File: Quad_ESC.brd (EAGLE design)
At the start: 96.5 x 39.9 mm, 28 parts, among them Y1 ECS-80-S-4X

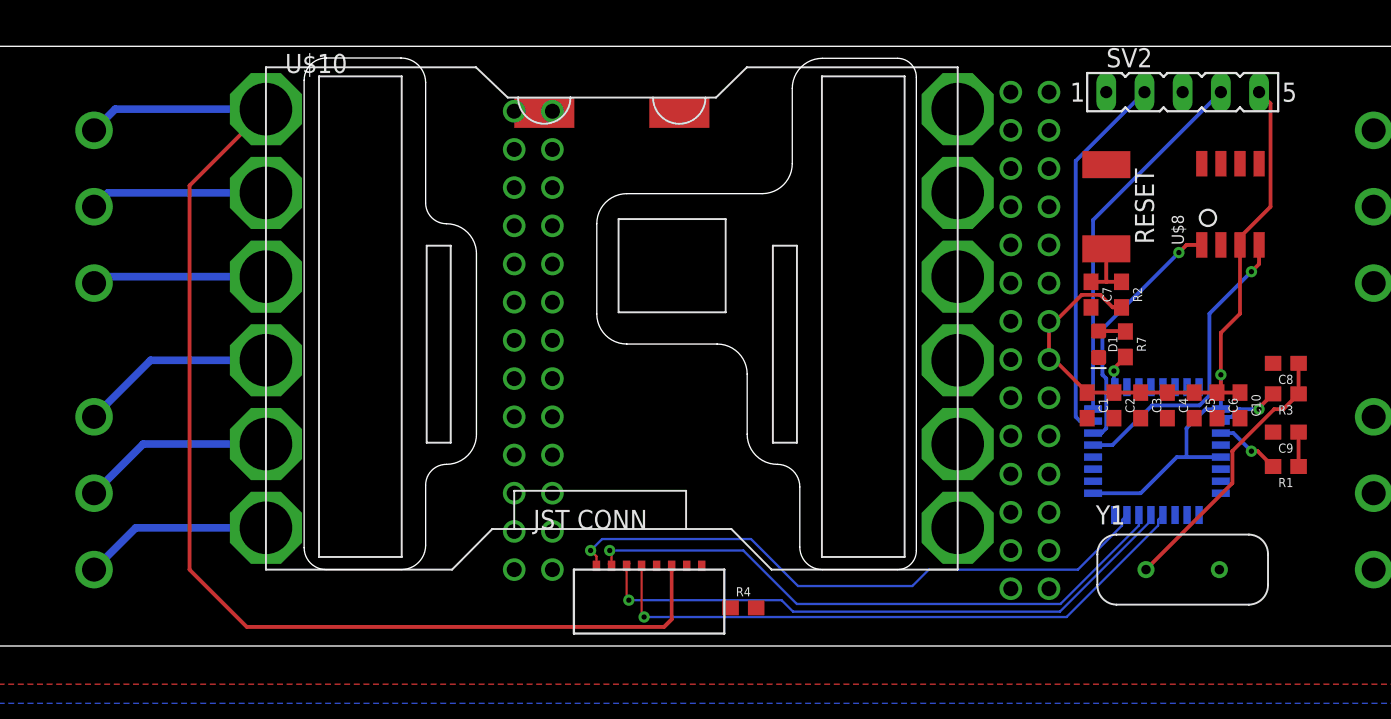
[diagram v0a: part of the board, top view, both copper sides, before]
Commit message: Quick Board Update
ripup; done for presentation, only placement of components present on board
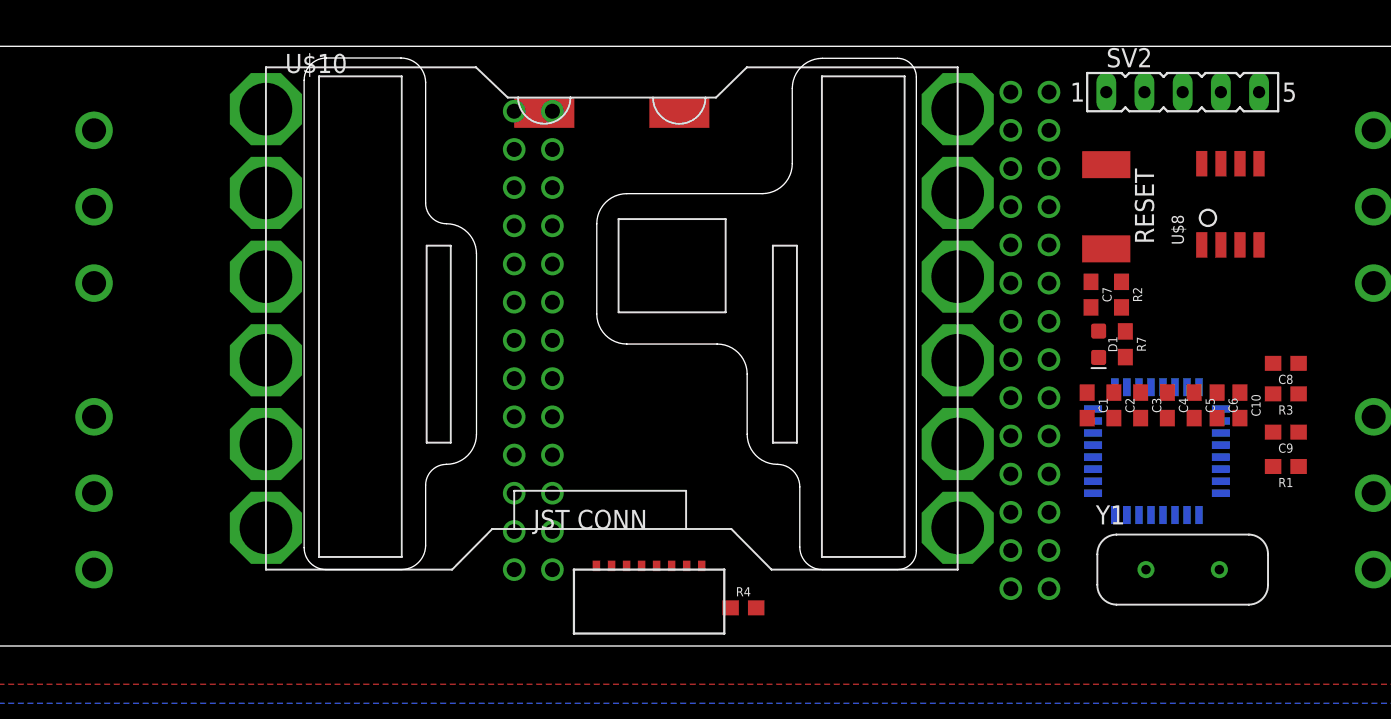
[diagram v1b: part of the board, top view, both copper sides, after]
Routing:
- net ESC1_B: track 82.1 -> 0.00 mm
- net +3V3: track 60.3 -> 0.00 mm, vias 1 -> 0
- net TIM3_CH1: track 41.0 -> 0.00 mm, vias 1 -> 0
- net TIM3_CH3: track 40.8 -> 0.00 mm, vias 1 -> 0
- net TIM3_CH4: track 40.6 -> 0.00 mm, vias 1 -> 0
- net TIM3_CH2: track 40.5 -> 0.00 mm, vias 1 -> 0
- net SWDIO: track 24.8 -> 0.00 mm
- net SWCLK: track 24.6 -> 0.00 mm
- net CAN_RX: track 20.5 -> 0.00 mm, vias 1 -> 0
- net N$2: track 18.3 -> 0.00 mm
- net CAN_TX: track 16.6 -> 0.00 mm, vias 1 -> 0
- net ESC2_B: track 13.0 -> 0.00 mm
- net ESC2_Y: track 12.8 -> 0.00 mm
- net ESC2_R: track 12.6 -> 0.00 mm
- net ESC1_Y: track 11.8 -> 0.00 mm
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
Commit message: Update Quad_ESC.brd
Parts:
- moved U$2 64.2 mm to (14.0, 3.05), turned to 180 degrees
- moved R4 36.2 mm to (85.3, 7.87)
- moved U$7 24.6 mm to (66.8, 10.2)
- moved U$6 24.4 mm to (67.1, 29.2)
- moved Y1 14.6 mm to (92.2, 10.7), turned to 270 degrees
- moved U$9 7.89 mm to (40.6, 7.11)
- moved U$10 4.44 mm to (13.5, 6.10)
- moved U$4 0.51 mm to (81.8, 10.2)
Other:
- board size 96.5 x 39.9 mm -> 96.5 x 40.1 mm

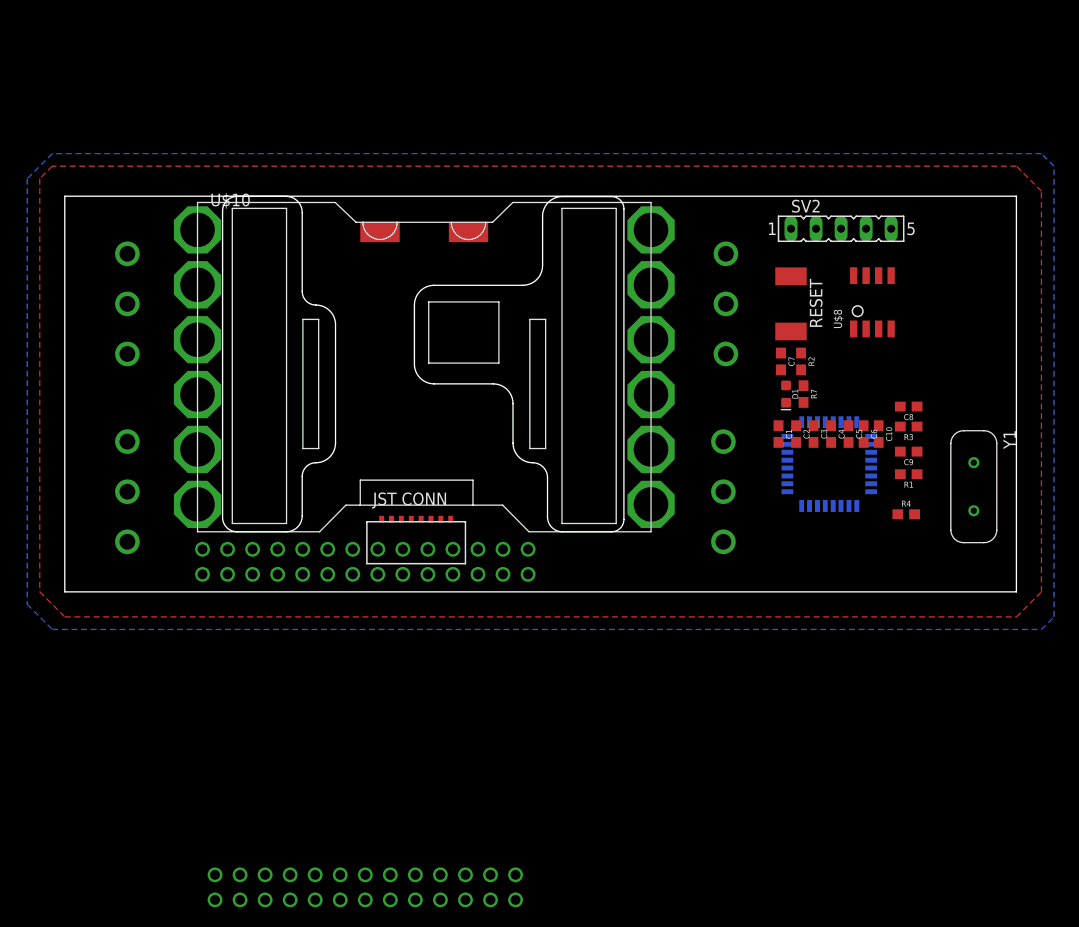
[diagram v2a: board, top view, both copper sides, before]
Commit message: Board/Schem Update
added CLT low profile samtec connectors to schem/board, looking at the connector spacing on the board stresses me out ;-;
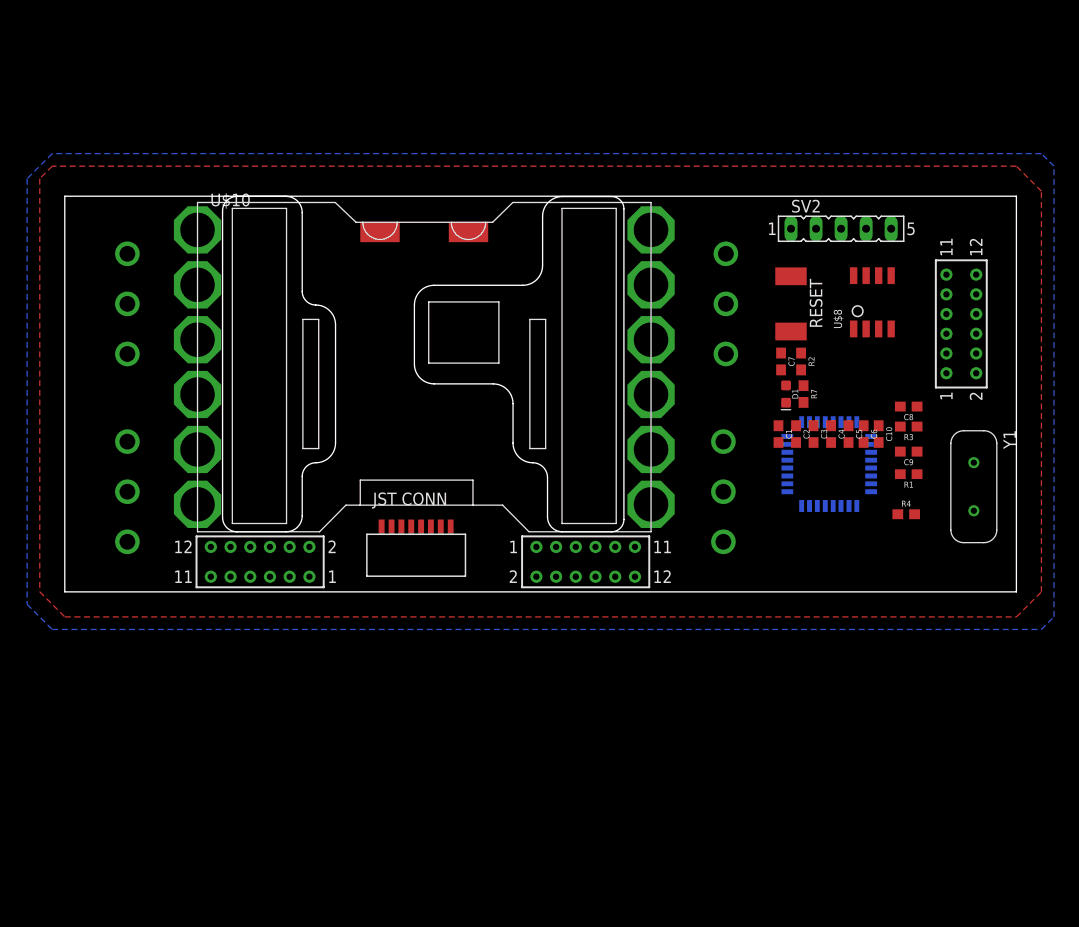
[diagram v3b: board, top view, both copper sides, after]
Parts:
- removed U$9: 8PIN_CONNECTOR, BLHeli_32 45A:8PI_CONNECTOR
- added J1, J2, J3: SAMTEC-CLT-106-01-X-DJ, BLHeli_32 45A:SAMTEC-CLT-106-01-X-D
- U$2: value ESC2BACKPLANE -> 8PIN_CONNECTOR; device ESC_to_Backplane_Connectors:ESC2BACKPLANE_WHOLE -> BLHeli_32 45A:8PI_CONNECTOR
- moved U$2 26.8 mm to (40.6, 5.84), flipped to the top
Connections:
- removed net N$10: U$2.P$7
- removed net N$6: U$9.P$4
- removed net N$9: U$2.P$6
- removed net PROG_SEL: U$2.P$5
- net +12V: now also J1.1, J1.2, J1.3, J1.4, J1.5, J1.6, J1.7, J1.8, J2.1, J2.2, J2.3, J2.4, J2.5, J2.6, J2.7, J2.8; no longer U$2.P$10, U$2.P$11, U$2.P$12, U$2.P$13, U$2.P$23, U$2.P$24, U$2.P$25, U$2.P$26, U$2.P$27, U$2.P$9, U$2.P$A, U$2.P$B, U$2.P$C, U$2.P$D, U$2.P$E, U$2.P$O, U$2.P$P, U$2.P$Q, U$2.P$R, U$2.P$S
- net +3V3: now also J3.1, J3.2, J3.3, J3.4; no longer U$2.P$G, U$2.P$H, U$2.P$U, U$2.P$V
- net CAN_H: now also J3.7
- net CAN_L: now also J3.9
- net ESC1_B: no longer U$9.P$3
- net GND: now also J1.10, J1.11, J1.12, J1.9, J2.10, J2.11, J2.12, J2.9; no longer U$2.P$1, U$2.P$15, U$2.P$16, U$2.P$17, U$2.P$18, U$2.P$2, U$2.P$3, U$2.P$4, U$2.P$AA, U$2.P$BB, U$2.P$J, U$2.P$K, U$2.P$L, U$2.P$M, U$2.P$N, U$2.P$X, U$2.P$Y, U$2.P$Z, U$9.P$1, U$9.P$2
- net TIM3_CH1: no longer U$9.P$5
- net TIM3_CH2: no longer U$9.P$6
- net TIM3_CH3: no longer U$9.P$7
- net TIM3_CH4: no longer U$9.P$8

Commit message: Board Update
actually put the connectors on the right side of the board this time haha
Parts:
- moved J2 0.76 mm to (19.1, 3.05), flipped to the bottom, turned to 0 degrees
- moved J3 0.57 mm to (91.4, 27.4), flipped to the bottom
- moved J1 0.25 mm to (53.1, 3.05), flipped to the bottom, turned to 180 degrees
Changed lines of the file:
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@@
 <attribute name="VALUE" x="85.344" y="7.112" size="0.6096" layer="27" font="vector" ratio="20" align="top-center"/>
 </element>
-<element name="J2" library="BLHeli_32 45A" package="SAMTEC-CLT-106-01-X-D" value="SAMTEC-CLT-106-01-X-DJ" x="19.812" y="3.048" smashed="yes" rot="R180">
-<attribute name="VALUE" x="19.812" y="3.748" size="0.635" layer="27" rot="R180" align="bottom-center"/>
-</element>
-<element name="J3" library="BLHeli_32 45A" package="SAMTEC-CLT-106-01-X-D" value="SAMTEC-CLT-106-01-X-DJ" x="90.932" y="27.178" smashed="yes" rot="R90">
-<attribute name="VALUE" x="91.632" y="27.178" size="0.635" layer="27" rot="R90" align="bottom-center"/>
+<element name="J2" library="BLHeli_32 45A" package="SAMTEC-CLT-106-01-X-D" value="SAMTEC-CLT-106-01-X-DJ" x="19.05" y="3.048" smashed="yes" rot="MR0">
+<attribute name="VALUE" x="19.05" y="2.348" size="0.635" layer="28" rot="MR0" align="bottom-center"/>
+</element>
+<element name="J3" library="BLHeli_32 45A" package="SAMTEC-CLT-106-01-X-D" value="SAMTEC-CLT-106-01-X-DJ" x="91.44" y="27.432" smashed="yes" rot="MR90">
+<attribute name="VALUE" x="90.74" y="27.432" size="0.635" layer="28" rot="MR90" align="bottom-center"/>
 </element>
 <element name="U$2" library="BLHeli_32 45A" package="8PI_CONNECTOR" value="8PIN_CONNECTOR" x="40.64" y="5.842" smashed="yes" rot="R180"/>
-<element name="J1" library="BLHeli_32 45A" package="SAMTEC-CLT-106-01-X-D" value="SAMTEC-CLT-106-01-X-DJ" x="52.832" y="3.048" smashed="yes">
-<attribute name="VALUE" x="53.086" y="2.348" size="0.635" layer="27" align="bottom-center"/>
+<element name="J1" library="BLHeli_32 45A" package="SAMTEC-CLT-106-01-X-D" value="SAMTEC-CLT-106-01-X-DJ" x="53.086" y="3.048" smashed="yes" rot="MR180">
+<attribute name="VALUE" x="53.34" y="3.748" size="0.635" layer="28" rot="MR180" align="bottom-center"/>
 </element>
 </elements>
@@
 <wire x1="86.194" y1="7.874" x2="80.338" y2="8.71" width="0" layer="19" extent="1-16"/>
 <wire x1="31.972" y1="36.466" x2="73.66" y2="32.01" width="0" layer="19" extent="1-1"/>
-<wire x1="14.812" y1="1.537" x2="31.972" y2="36.466" width="0" layer="19" extent="1-1"/>
-<wire x1="16.812" y1="1.537" x2="14.812" y2="1.537" width="0" layer="19" extent="1-1"/>
-<wire x1="16.812" y1="4.559" x2="16.812" y2="1.537" width="0" layer="19" extent="1-1"/>
-<wire x1="14.812" y1="4.559" x2="16.812" y2="4.559" width="0" layer="19" extent="1-1"/>
-<wire x1="55.832" y1="4.559" x2="16.812" y2="4.559" width="0" layer="19" extent="1-1"/>
-<wire x1="57.832" y1="4.559" x2="55.832" y2="4.559" width="0" layer="19" extent="1-1"/>
-<wire x1="55.832" y1="1.537" x2="55.832" y2="4.559" width="0" layer="19" extent="1-1"/>
-<wire x1="57.832" y1="1.537" x2="55.832" y2="1.537" width="0" layer="19" extent="1-1"/>
+<wire x1="14.05" y1="4.559" x2="31.972" y2="36.466" width="0" layer="19" extent="1-1"/>
+<wire x1="16.05" y1="4.559" x2="14.05" y2="4.559" width="0" layer="19" extent="1-1"/>
+<wire x1="16.05" y1="1.537" x2="16.05" y2="4.559" width="0" layer="19" extent="1-1"/>
+<wire x1="14.05" y1="1.537" x2="16.05" y2="1.537" width="0" layer="19" extent="1-1"/>
+<wire x1="56.086" y1="1.537" x2="16.05" y2="1.537" width="0" layer="19" extent="1-1"/>
+<wire x1="58.086" y1="1.537" x2="56.086" y2="1.537" width="0" layer="19" extent="1-1"/>
+<wire x1="56.086" y1="4.559" x2="56.086" y2="1.537" width="0" layer="19" extent="1-1"/>
+<wire x1="58.086" y1="4.559" x2="56.086" y2="4.559" width="0" layer="19" extent="1-1"/>
 </signal>
 <signal name="+3V3">
@@
 <wire x1="81.788" y1="12.56" x2="81.788" y2="15.76" width="0" layer="19" extent="16-16"/>
 <wire x1="73.288" y1="10.16" x2="74.168" y2="16.852" width="0" layer="19" extent="1-16"/>
-<wire x1="89.421" y1="24.178" x2="73.288" y2="10.16" width="0" layer="19" extent="16-16"/>
-<wire x1="89.421" y1="22.178" x2="89.421" y2="24.178" width="0" layer="19" extent="1-1"/>
-<wire x1="92.443" y1="22.178" x2="89.421" y2="22.178" width="0" layer="19" extent="1-1"/>
-<wire x1="92.443" y1="24.178" x2="92.443" y2="22.178" width="0" layer="19" extent="1-1"/>
+<wire x1="92.951" y1="24.432" x2="73.288" y2="10.16" width="0" layer="19" extent="16-16"/>
+<wire x1="92.951" y1="22.432" x2="92.951" y2="24.432" width="0" layer="19" extent="1-1"/>
+<wire x1="89.929" y1="22.432" x2="92.951" y2="22.432" width="0" layer="19" extent="1-1"/>
+<wire x1="89.929" y1="24.432" x2="89.929" y2="22.432" width="0" layer="19" extent="1-1"/>
 </signal>
 <signal name="CAN_TX">
@@
 <contactref element="J1" pad="5"/>
 <contactref element="J1" pad="7"/>
-<wire x1="18.812" y1="1.537" x2="40.952" y2="36.466" width="0" layer="19" extent="1-1"/>
-<wire x1="20.812" y1="1.537" x2="18.812" y2="1.537" width="0" layer="19" extent="1-1"/>
-<wire x1="22.812" y1="1.537" x2="20.812" y2="1.537" width="0" layer="19" extent="1-1"/>
-<wire x1="24.812" y1="1.537" x2="22.812" y2="1.537" width="0" layer="19" extent="1-1"/>
-<wire x1="24.812" y1="4.559" x2="24.812" y2="1.537" width="0" layer="19" extent="1-1"/>
-<wire x1="22.812" y1="4.559" x2="24.812" y2="4.559" width="0" layer="19" extent="1-1"/>
-<wire x1="20.812" y1="4.559" x2="22.812" y2="4.559" width="0" layer="19" extent="1-1"/>
-<wire x1="18.812" y1="4.559" x2="20.812" y2="4.559" width="0" layer="19" extent="1-1"/>
-<wire x1="47.832" y1="4.559" x2="24.812" y2="4.559" width="0" layer="19" extent="1-1"/>
-<wire x1="49.832" y1="4.559" x2="47.832" y2="4.559" width="0" layer="19" extent="1-1"/>
-<wire x1="51.832" y1="4.559" x2="49.832" y2="4.559" width="0" layer="19" extent="1-1"/>
-<wire x1="53.832" y1="4.559" x2="51.832" y2="4.559" width="0" layer="19" extent="1-1"/>
-<wire x1="47.832" y1="1.537" x2="47.832" y2="4.559" width="0" layer="19" extent="1-1"/>
-<wire x1="49.832" y1="1.537" x2="47.832" y2="1.537" width="0" layer="19" extent="1-1"/>
-<wire x1="51.832" y1="1.537" x2="49.832" y2="1.537" width="0" layer="19" extent="1-1"/>
-<wire x1="53.832" y1="1.537" x2="51.832" y2="1.537" width="0" layer="19" extent="1-1"/>
+<wire x1="18.05" y1="4.559" x2="40.952" y2="36.466" width="0" layer="19" extent="1-1"/>
+<wire x1="20.05" y1="4.559" x2="18.05" y2="4.559" width="0" layer="19" extent="1-1"/>
+<wire x1="22.05" y1="4.559" x2="20.05" y2="4.559" width="0" layer="19" extent="1-1"/>
+<wire x1="24.05" y1="4.559" x2="22.05" y2="4.559" width="0" layer="19" extent="1-1"/>
+<wire x1="24.05" y1="1.537" x2="24.05" y2="4.559" width="0" layer="19" extent="1-1"/>
+<wire x1="22.05" y1="1.537" x2="24.05" y2="1.537" width="0" layer="19" extent="1-1"/>
+<wire x1="20.05" y1="1.537" x2="22.05" y2="1.537" width="0" layer="19" extent="1-1"/>
+<wire x1="18.05" y1="1.537" x2="20.05" y2="1.537" width="0" layer="19" extent="1-1"/>
+<wire x1="48.086" y1="1.537" x2="24.05" y2="1.537" width="0" layer="19" extent="1-1"/>
+<wire x1="50.086" y1="1.537" x2="48.086" y2="1.537" width="0" layer="19" extent="1-1"/>
+<wire x1="52.086" y1="1.537" x2="50.086" y2="1.537" width="0" layer="19" extent="1-1"/>
+<wire x1="54.086" y1="1.537" x2="52.086" y2="1.537" width="0" layer="19" extent="1-1"/>
+<wire x1="48.086" y1="4.559" x2="48.086" y2="1.537" width="0" layer="19" extent="1-1"/>
+<wire x1="50.086" y1="4.559" x2="48.086" y2="4.559" width="0" layer="19" extent="1-1"/>
+<wire x1="52.086" y1="4.559" x2="50.086" y2="4.559" width="0" layer="19" extent="1-1"/>
+<wire x1="54.086" y1="4.559" x2="52.086" y2="4.559" width="0" layer="19" extent="1-1"/>
 </signal>
 <signal name="TIM3_CH1">
@@
 <contactref element="U$8" pad="CANH"/>
 <contactref element="J3" pad="7"/>
-<wire x1="89.421" y1="28.178" x2="81.28" y2="32.07" width="0" layer="19" extent="1-1"/>
+<wire x1="92.951" y1="28.432" x2="81.28" y2="32.07" width="0" layer="19" extent="1-1"/>
 </signal>
 <signal name="CAN_L">
 <contactref element="U$8" pad="CANL"/>
 <contactref element="J3" pad="9"/>
-<wire x1="89.421" y1="30.178" x2="82.55" y2="32.07" width="0" layer="19" extent="1-1"/>
+<wire x1="92.951" y1="30.432" x2="82.55" y2="32.07" width="0" layer="19" extent="1-1"/>
 </signal>
 <signal name="SWDIO">
